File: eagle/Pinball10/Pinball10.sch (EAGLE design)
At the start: 49 parts, among them J1 UB-M5BR-DM14, M0+ m, M1+ m, Q1 MOSFET-NCHANNEL2N7002PW, U1 CYBLE-014008-00, U2 MMA8452Q, U3 PCA9306, U4 V_REG_317SMD

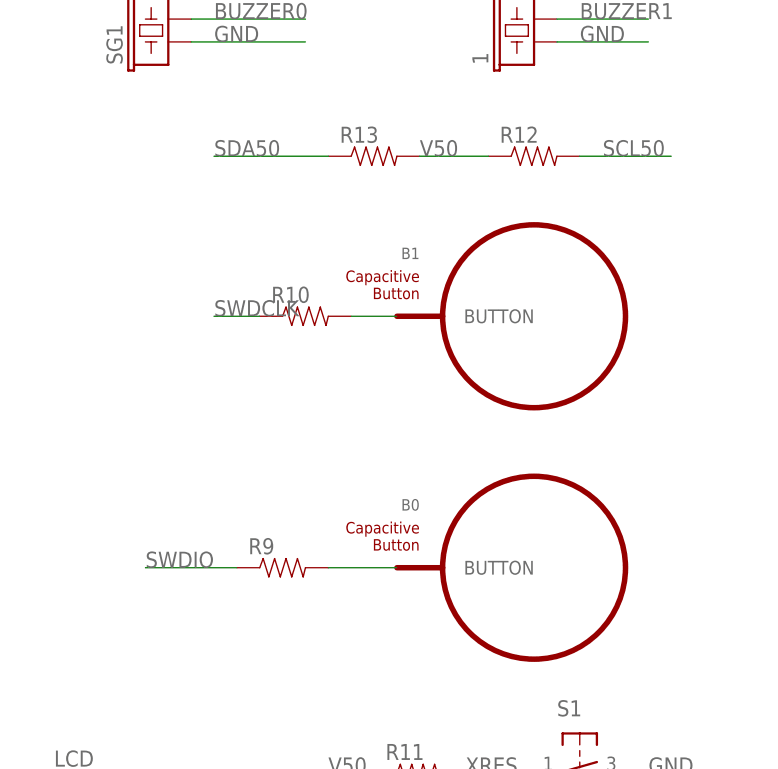
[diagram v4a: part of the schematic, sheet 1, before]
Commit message: added some values to the schematic as I filled in the BOM
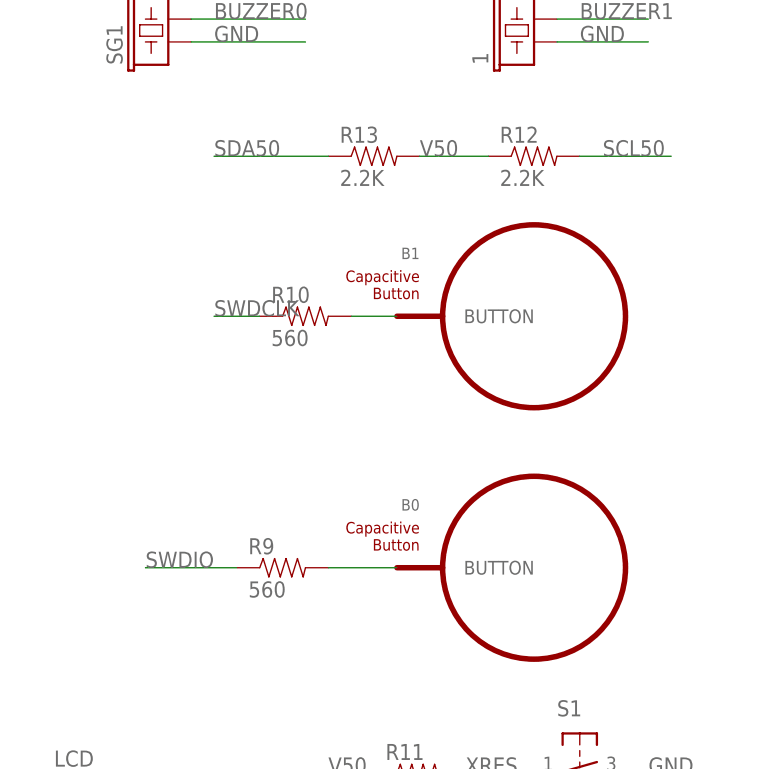
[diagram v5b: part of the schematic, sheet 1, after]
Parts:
- C1: value (none) -> 0.1uF
- C2: value (none) -> 1uF
- R1, R2, R3, R4: value (none) -> 330
- R10, R9: value (none) -> 560
- R12, R13: value (none) -> 2.2K
- R5: value (none) -> 1.8K
- R6: value (none) -> 1.2K
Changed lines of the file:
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@@
 <part name="J1" library="con-usb" deviceset="UB-M5BR-DM14" device=""/>
 <part name="BANK0" library="SparkFun-Connectors" deviceset="M08X2" device="" value="M08X2"/>
-<part name="R1" library="SparkFun" deviceset="RESISTOR" device=""/>
-<part name="R2" library="SparkFun" deviceset="RESISTOR" device=""/>
-<part name="R3" library="SparkFun" deviceset="RESISTOR" device=""/>
-<part name="R4" library="SparkFun" deviceset="RESISTOR" device=""/>
+<part name="R1" library="SparkFun" deviceset="RESISTOR" device="" value="330"/>
+<part name="R2" library="SparkFun" deviceset="RESISTOR" device="" value="330"/>
+<part name="R3" library="SparkFun" deviceset="RESISTOR" device="" value="330"/>
+<part name="R4" library="SparkFun" deviceset="RESISTOR" device="" value="330"/>
 <part name="LEDBANK1" library="SparkFun-Connectors" deviceset="M08X2" device=""/>
 <part name="D1" library="SparkFun-DiscreteSemi" deviceset="DIODE" device="SOD"/>
@@
 <part name="U2" library="SparkFun-Sensors" deviceset="MMA8452Q" device=""/>
 <part name="U3" library="SparkFun-DigitalIC" deviceset="PCA9306" device="" value="PCA9306"/>
-<part name="R5" library="SparkFun-Passives" deviceset="RESISTOR" device="0805-RES"/>
-<part name="R6" library="SparkFun-Passives" deviceset="RESISTOR" device="0805-RES"/>
+<part name="R5" library="SparkFun-Passives" deviceset="RESISTOR" device="0805-RES" value="1.8K"/>
+<part name="R6" library="SparkFun-Passives" deviceset="RESISTOR" device="0805-RES" value="1.2K"/>
 <part name="U4" library="SparkFun-PowerIC" deviceset="V_REG_317" device="SMD"/>
-<part name="C1" library="SparkFun-Capacitors" deviceset="CAP" device="0805"/>
-<part name="C2" library="SparkFun-Capacitors" deviceset="CAP" device="0805"/>
+<part name="C1" library="SparkFun-Capacitors" deviceset="CAP" device="0805" value="0.1uF"/>
+<part name="C2" library="SparkFun-Capacitors" deviceset="CAP" device="0805" value="1uF"/>
 <part name="Q1" library="SparkFun-DiscreteSemi" deviceset="MOSFET-NCHANNEL" device="2N7002PW"/>
 <part name="R7" library="SparkFun-Passives" deviceset="RESISTOR" device="0805-RES" value="10K"/>
@@
 <part name="C4" library="SparkFun-Capacitors" deviceset="CAP" device="0805" value="0.1uF"/>
 <part name="C5" library="SparkFun-Capacitors" deviceset="CAP" device="0805" value="4.7uF"/>
-<part name="R9" library="SparkFun-Passives" deviceset="RESISTOR" device="0805-RES"/>
-<part name="R10" library="SparkFun-Passives" deviceset="RESISTOR" device="0805-RES"/>
+<part name="R9" library="SparkFun-Passives" deviceset="RESISTOR" device="0805-RES" value="560"/>
+<part name="R10" library="SparkFun-Passives" deviceset="RESISTOR" device="0805-RES" value="560"/>
 <part name="R11" library="SparkFun-Resistors" deviceset="RESISTOR" device="0805-RES"/>
 <part name="S1" library="SparkFun-Electromechanical" deviceset="TAC_SWITCH" device="SMD" value="TAC_SWITCHSMD"/>
@@
 <part name="M1+" library="SparkFun-Connectors" deviceset="M02" device="PTH" value="m"/>
 <part name="JP3" library="SparkFun-Connectors" deviceset="M05" device="LOCK"/>
-<part name="R12" library="SparkFun-Passives" deviceset="RESISTOR" device="0805-RES"/>
-<part name="R13" library="SparkFun-Passives" deviceset="RESISTOR" device="0805-RES"/>
+<part name="R12" library="SparkFun-Passives" deviceset="RESISTOR" device="0805-RES" value="2.2K"/>
+<part name="R13" library="SparkFun-Passives" deviceset="RESISTOR" device="0805-RES" value="2.2K"/>
 <part name="V50" library="testpad" deviceset="PTR1" device="PAD1-13"/>
 <part name="GND" library="testpad" deviceset="PTR1" device="PAD1-13" value="GND"/>
@@
 <sheets>
 <sheet>
+<description>Main</description>
 <plain>
 </plain>

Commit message: the board ... but with the crash
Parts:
- M1+: value m -> M02PTH
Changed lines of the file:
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@@
 <?xml version="1.0" encoding="utf-8"?>
 <!DOCTYPE eagle SYSTEM "eagle.dtd">
-<eagle version="7.6.0">
+<eagle version="7.7.0">
 <drawing>
 <settings>
@@
 <class number="0" name="default" width="0" drill="0">
 </class>
-<class number="1" name="power" width="1.016" drill="0">
+<class number="1" name="power" width="0.1524" drill="0">
 </class>
 </classes>
@@
 <part name="S1" library="SparkFun-Electromechanical" deviceset="TAC_SWITCH" device="SMD" value="TAC_SWITCHSMD"/>
 <part name="M0+" library="SparkFun-Connectors" deviceset="M02" device="PTH" value="m"/>
-<part name="M1+" library="SparkFun-Connectors" deviceset="M02" device="PTH" value="m"/>
+<part name="M1+" library="SparkFun-Connectors" deviceset="M02" device="PTH" value="M02PTH"/>
 <part name="JP3" library="SparkFun-Connectors" deviceset="M05" device="LOCK"/>
 <part name="R12" library="SparkFun-Passives" deviceset="RESISTOR" device="0805-RES" value="2.2K"/>

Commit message: completed 1.1 of board
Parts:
- removed J1: UB-M5BR-DM14, con-usb:UB-M5BR-DM14
- added X1: MINI-USB-SHIELD-UX60-MB-5S8, con-hirose:MINI-USB-SHIELD-UX60-MB-5S8
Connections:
- net GND: now also X1G$1.5; no longer J1.GND
- net V50: now also X1G$1.1; no longer J1.VBUS
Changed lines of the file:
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@@
 <part name="HBRIDGE" library="SparkFun" deviceset="TB6621FNG" device=""/>
 <part name="U$1" library="arh" deviceset="9X2" device=""/>
-<part name="J1" library="con-usb" deviceset="UB-M5BR-DM14" device=""/>
 <part name="BANK0" library="SparkFun-Connectors" deviceset="M08X2" device="" value="M08X2"/>
 <part name="R1" library="SparkFun" deviceset="RESISTOR" device="" value="330"/>
@@
 <part name="GND" library="testpad" deviceset="PTR1" device="PAD1-13" value="GND"/>
 <part name="V33" library="testpad" deviceset="PTR1" device="PAD1-13"/>
+<part name="X1" library="con-hirose" deviceset="MINI-USB-SHIELD-" device="UX60-MB-5S8"/>
 </parts>
 <sheets>
@@
 <instances>
 <instance part="U1" gate="U1" x="38.1" y="50.8"/>
-<instance part="J1" gate="G$1" x="48.26" y="99.06"/>
 <instance part="SG1" gate="G$1" x="88.9" y="88.9" rot="R90"/>
 <instance part="1" gate="G$1" x="129.54" y="88.9" rot="R90"/>
@@
 <instance part="R12" gate="G$1" x="129.54" y="76.2"/>
 <instance part="R13" gate="G$1" x="111.76" y="76.2"/>
+<instance part="X1" gate="G$1" x="45.72" y="99.06"/>
 </instances>
 <busses>
@@
 </segment>
 <segment>
-<pinref part="J1" gate="G$1" pin="GND"/>
 <wire x1="40.64" y1="93.98" x2="25.4" y2="93.98" width="0.1524" layer="91"/>
 <label x="25.4" y="93.98" size="1.778" layer="95"/>
+<pinref part="X1" gate="G$1" pin="5"/>
 </segment>
 <segment>
@@
 <net name="V50" class="1">
 <segment>
-<pinref part="J1" gate="G$1" pin="VBUS"/>
 <wire x1="40.64" y1="104.14" x2="25.4" y2="104.14" width="0.1524" layer="91"/>
 <label x="25.4" y="104.14" size="1.778" layer="95"/>
-</segment>
-<segment>
+<pinref part="X1" gate="G$1" pin="1"/>
+</segment>
+<segment>

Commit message: New layout
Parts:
- removed LCD: (no value), SparkFun-Connectors:M04JST-PTH
- removed Q1: MOSFET-NCHANNEL2N7002PW, SparkFun-DiscreteSemi:MOSFET-NCHANNEL2N7002PW
- removed R7, R8: 10K, SparkFun-Passives:RESISTOR0805-RES
- removed U3: PCA9306, SparkFun-DigitalIC:PCA9306
- added JP1: (no value), SparkFun-Connectors:M03PTH
- added U$2: U8G-096-OLED, IOTExpert:U8G-096-OLED
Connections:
- removed net N$4: Q1.S, R7.1, U2.INT1
- removed net SCL33: U2.SCL, U3.SCL2
- removed net SCL50: LCD.4, R12.2, U1.P0.5/SCL0, U3.SCL1
- removed net SDA33: U2.SDA, U3.SDA2
- removed net SDA50: LCD.3, R13.1, U1.P0.4/SDA0, U3.SDA1
- new net ACCEINT: U2.INT1
- new net SCL: R12.2, U$2.SCL, U1.P0.5/SCL0, U2.SCL
- new net SDA: R13.1, U$2.SDA, U1.P0.4/SDA0, U2.SDA
- new net VDD: U$2.VDD
- new net VMOTOR: HBRIDGE.VM1, HBRIDGE.VM2, HBRIDGE.VM3, JP1.2
- net ACCELINT: no longer Q1.D, R8.1
- net GND: now also U$2.GND; no longer LCD.1, U3.GND
- net V33: now also HBRIDGE.PWMA, HBRIDGE.PWMB, HBRIDGE.STBY, HBRIDGE.VCC, JP1.3, R11.1, R12.1, R13.2, U1.VDD, U1.VDDA, U1.VDDR; no longer Q1.G, R7.2, U3.EN, U3.VREF2
- net V50: now also JP1.1; no longer HBRIDGE.PWMA, HBRIDGE.PWMB, HBRIDGE.STBY, HBRIDGE.VCC, HBRIDGE.VM1, HBRIDGE.VM2, HBRIDGE.VM3, LCD.2, R11.1, R12.1, R13.2, R8.2, U1.VDD, U1.VDDA, U1.VDDR, U3.VREF1
